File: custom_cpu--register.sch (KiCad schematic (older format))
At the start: 45 parts, among them P1 CONN_01X01, P10 CONN_01X01, P11 CONN_01X01, P12 CONN_01X01, P13 CONN_01X01, P14 CONN_01X01, P15 CONN_01X01, P16 CONN_01X01, P17 CONN_01X01, P18 CONN_01X01, P19 CONN_01X01, P2 CONN_01X01, P20 CONN_01X01, P21 CONN_01X01, P22 CONN_01X01, P23 CONN_01X01, P24 CONN_01X01, P25 CONN_01X01, P3 CONN_01X01, P4 CONN_01X01, P5 CONN_01X01, P6 CONN_01X01, P7 CONN_01X01, P8 CONN_01X01, P9 CONN_01X01, U1 74LS173, U2 74LS173, U3 74LS245

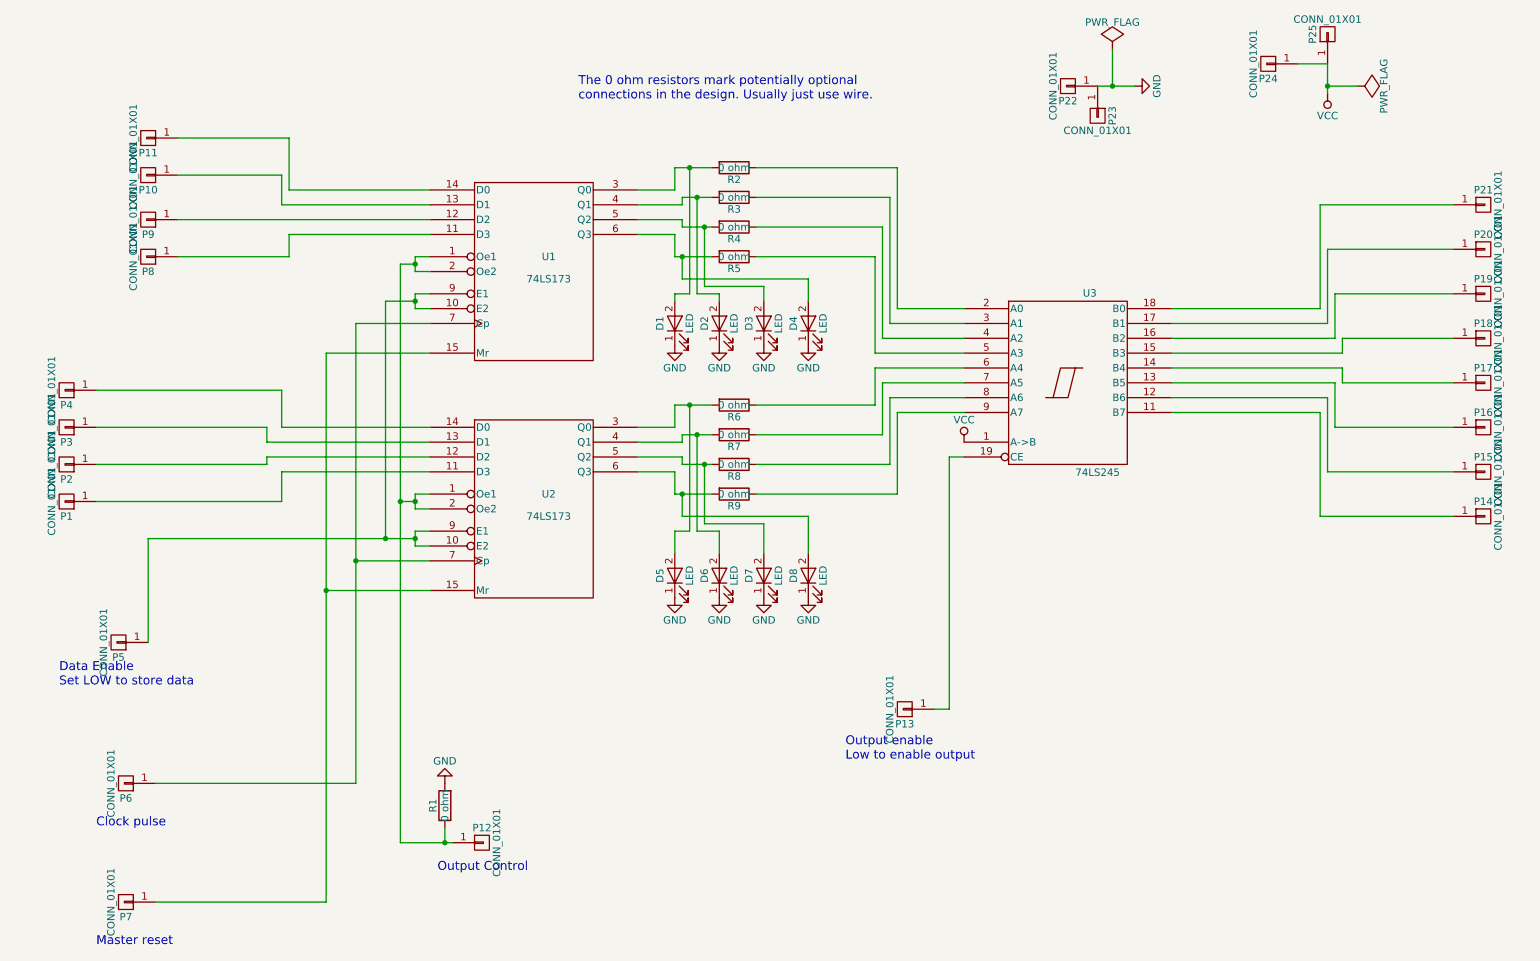
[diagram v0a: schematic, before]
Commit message: Make labels consistent with original design, add README
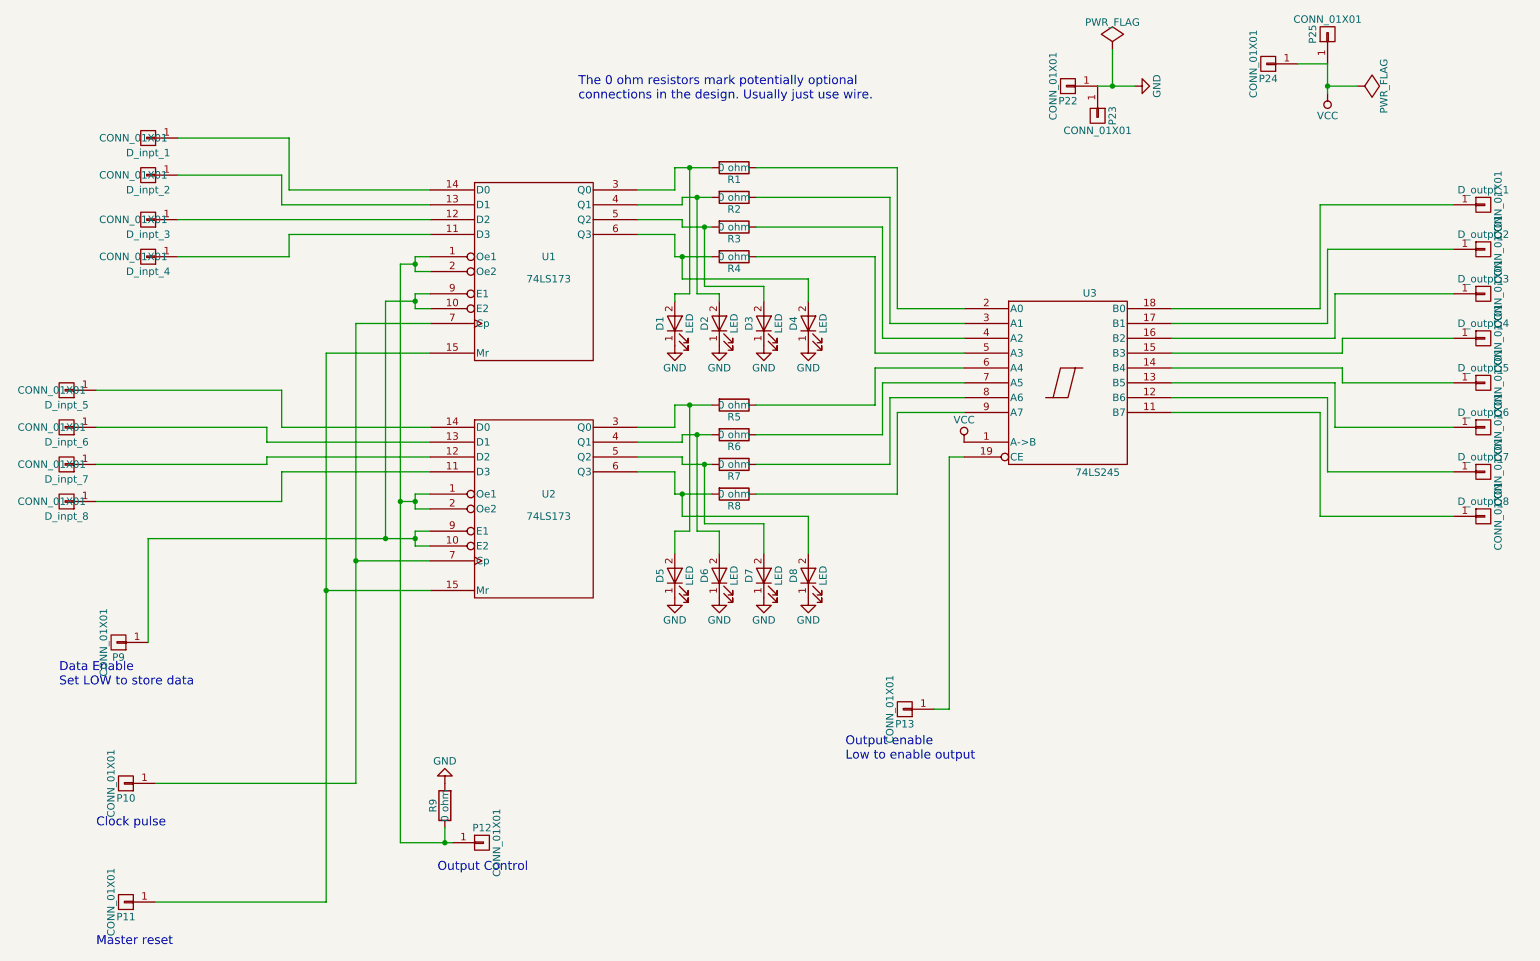
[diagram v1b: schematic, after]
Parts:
- renumbered P11 to D_inpt_1, P10 to D_inpt_2, P9 to D_inpt_3, P8 to D_inpt_4, P4 to D_inpt_5, P3 to D_inpt_6, P2 to D_inpt_7, P1 to D_inpt_8, P21 to D_outpt_1, P20 to D_outpt_2, P19 to D_outpt_3, P18 to D_outpt_4, P17 to D_outpt_5, P16 to D_outpt_6, P15 to D_outpt_7, P14 to D_outpt_8, P6 to P10, P7 to P11, P5 to P9, R2 to R1, R3 to R2, R4 to R3, R5 to R4, R6 to R5, R7 to R6, R8 to R7, R9 to R8, R1 to R9

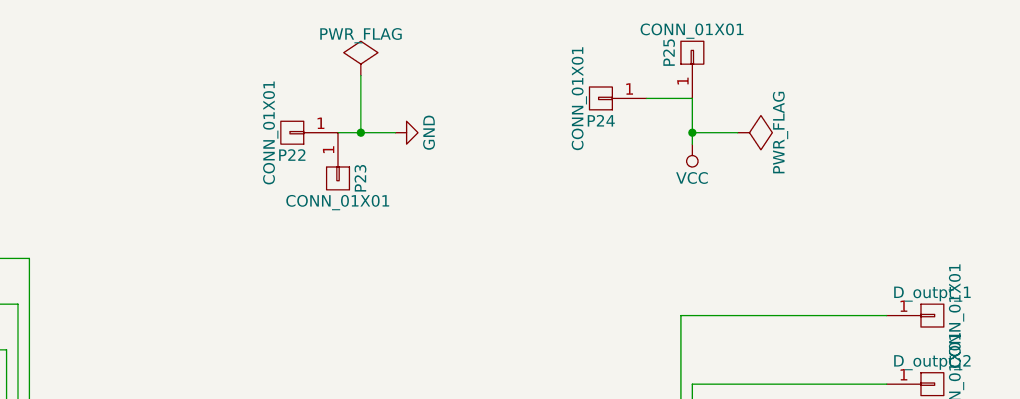
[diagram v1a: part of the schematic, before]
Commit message: Added redundant power pads to back of board
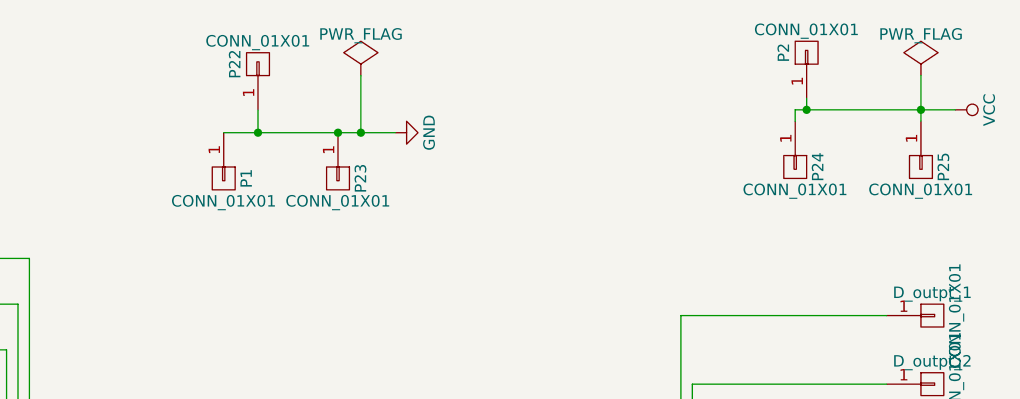
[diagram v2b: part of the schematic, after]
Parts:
- added P1, P2: CONN_01X01, Wire_Pads:SolderWirePad_single_SMD_5x10mm, symbol CONN_01X01
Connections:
- net GND: now also P1.1 (P1)
- net VCC: now also P2.1 (P1)
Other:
- moved on the sheet: P22, P24, P25
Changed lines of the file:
@@
 $EndComp
 $Comp
-L GND #PWR1
+L GND #PWR01
 U 1 1 58E818E9
 P 3300 5750
-F 0 "#PWR1" H 3300 5500 50  0001 C CNN
+F 0 "#PWR01" H 3300 5500 50  0001 C CNN
 F 1 "GND" H 3300 5600 50  0000 C CNN
 F 2 "" H 3300 5750 50  0000 C CNN
@@
 $EndComp
 $Comp
-L VCC #PWR10
+L VCC #PWR02
 U 1 1 58E831EF
 P 6800 3450
-F 0 "#PWR10" H 6800 3300 50  0001 C CNN
+F 0 "#PWR02" H 6800 3300 50  0001 C CNN
 F 1 "VCC" H 6800 3600 50  0000 C CNN
 F 2 "" H 6800 3450 50  0000 C CNN
@@
 $EndComp
 $Comp
-L GND #PWR11
+L GND #PWR03
 U 1 1 58E81990
 P 7950 1050
-F 0 "#PWR11" H 7950 800 50  0001 C CNN
+F 0 "#PWR03" H 7950 800 50  0001 C CNN
 F 1 "GND" H 7950 900 50  0000 C CNN
 F 2 "" H 7950 1050 50  0000 C CNN
@@
 L CONN_01X01 P22
 U 1 1 58E81B2E
-P 7500 1050
-F 0 "P22" H 7500 1150 50  0000 C CNN
-F 1 "CONN_01X01" V 7600 1050 50  0000 C CNN
-F 2 "Connectors:PINTST" H 7500 1050 50  0001 C CNN
-F 3 "" H 7500 1050 50  0000 C CNN
-	1    7500 1050
-	-1   0    0    1
+P 7350 750
+F 0 "P22" H 7350 850 50  0000 C CNN
+F 1 "CONN_01X01" V 7450 750 50  0000 C CNN
+F 2 "Connectors:PINTST" H 7350 750 50  0001 C CNN
+F 3 "" H 7350 750 50  0000 C CNN
+	1    7350 750
+	0    -1   -1   0
 $EndComp
 $Comp
@@
 $EndComp
 $Comp
-L PWR_FLAG #FLG2
+L PWR_FLAG #FLG04
 U 1 1 58E81EC9
-P 9450 1050
-F 0 "#FLG2" H 9450 1145 50  0001 C CNN
-F 1 "PWR_FLAG" H 9450 1230 50  0000 C CNN
-F 2 "" H 9450 1050 50  0000 C CNN
-F 3 "" H 9450 1050 50  0000 C CNN
-	1    9450 1050
-	0    1    1    0
+P 10250 800
+F 0 "#FLG04" H 10250 895 50  0001 C CNN
+F 1 "PWR_FLAG" H 10250 980 50  0000 C CNN
+F 2 "" H 10250 800 50  0000 C CNN
+F 3 "" H 10250 800 50  0000 C CNN
+	1    10250 800
+	1    0    0    -1
 $EndComp
 $Comp
 L CONN_01X01 P25
 U 1 1 58E81F44
-P 9250 700
-F 0 "P25" H 9250 800 50  0000 C CNN
-F 1 "CONN_01X01" V 9350 700 50  0000 C CNN
-F 2 "Wire_Pads:SolderWirePad_single_SMD_5x10mm" H 9250 700 50  0001 C CNN
-F 3 "" H 9250 700 50  0000 C CNN
-	1    9250 700
-	0    -1   -1   0
+P 10250 1200
+F 0 "P25" H 10250 1300 50  0000 C CNN
+F 1 "CONN_01X01" V 10350 1200 50  0000 C CNN
+F 2 "Wire_Pads:SolderWirePad_single_SMD_5x10mm" H 10250 1200 50  0001 C CNN
+F 3 "" H 10250 1200 50  0000 C CNN
+	1    10250 1200
+	0    1    1    0
 $EndComp
 $Comp
 L CONN_01X01 P24
 U 1 1 58E82042
-P 8850 900
-F 0 "P24" H 8850 1000 50  0000 C CNN
-F 1 "CONN_01X01" V 8950 900 50  0000 C CNN
-F 2 "Connectors:PINTST" H 8850 900 50  0001 C CNN
-F 3 "" H 8850 900 50  0000 C CNN
-	1    8850 900
-	-1   0    0    1
-$EndComp
-$Comp
-L VCC #PWR12
+P 9700 1200
+F 0 "P24" H 9700 1300 50  0000 C CNN
+F 1 "CONN_01X01" V 9800 1200 50  0000 C CNN
+F 2 "Connectors:PINTST" H 9700 1200 50  0001 C CNN
+F 3 "" H 9700 1200 50  0000 C CNN
+	1    9700 1200
+	0    1    1    0
+$EndComp
+$Comp
+L VCC #PWR05
 U 1 1 58E820DA
-P 9250 1100
-F 0 "#PWR12" H 9250 950 50  0001 C CNN
-F 1 "VCC" H 9250 1250 50  0000 C CNN
-F 2 "" H 9250 1100 50  0000 C CNN
-F 3 "" H 9250 1100 50  0000 C CNN
-	1    9250 1100
-	-1   0    0    1
-$EndComp
-$Comp
-L PWR_FLAG #FLG1
+P 10400 950
+F 0 "#PWR05" H 10400 800 50  0001 C CNN
+F 1 "VCC" H 10400 1100 50  0000 C CNN
+F 2 "" H 10400 950 50  0000 C CNN
+F 3 "" H 10400 950 50  0000 C CNN
+	1    10400 950
+	0    1    1    0
+$EndComp
+$Comp
+L PWR_FLAG #FLG06
 U 1 1 58E8410D
 P 7800 800
-F 0 "#FLG1" H 7800 895 50  0001 C CNN
+F 0 "#FLG06" H 7800 895 50  0001 C CNN
 F 1 "PWR_FLAG" H 7800 980 50  0000 C CNN
 F 2 "" H 7800 800 50  0000 C CNN
@@
 $EndComp
 $Comp
-L GND #PWR2
+L GND #PWR07
 U 1 1 58E89432
 P 4850 2800
-F 0 "#PWR2" H 4850 2550 50  0001 C CNN
+F 0 "#PWR07" H 4850 2550 50  0001 C CNN
 F 1 "GND" H 4850 2650 50  0000 C CNN
 F 2 "" H 4850 2800 50  0000 C CNN
@@
 $EndComp
 $Comp
-L GND #PWR4
+L GND #PWR08
 U 1 1 58E894C4
 P 5150 2800
-F 0 "#PWR4" H 5150 2550 50  0001 C CNN
+F 0 "#PWR08" H 5150 2550 50  0001 C CNN
 F 1 "GND" H 5150 2650 50  0000 C CNN
 F 2 "" H 5150 2800 50  0000 C CNN
@@
 $EndComp
 $Comp
-L GND #PWR6
+L GND #PWR09
 U 1 1 58E89556
 P 5450 2800
-F 0 "#PWR6" H 5450 2550 50  0001 C CNN
+F 0 "#PWR09" H 5450 2550 50  0001 C CNN
 F 1 "GND" H 5450 2650 50  0000 C CNN
 F 2 "" H 5450 2800 50  0000 C CNN
@@
 $EndComp
 $Comp
-L GND #PWR8
+L GND #PWR010
 U 1 1 58E895E8
 P 5750 2800
-F 0 "#PWR8" H 5750 2550 50  0001 C CNN
+F 0 "#PWR010" H 5750 2550 50  0001 C CNN
 F 1 "GND" H 5750 2650 50  0000 C CNN
 F 2 "" H 5750 2800 50  0000 C CNN
@@
 $EndComp
 $Comp
-L GND #PWR9
+L GND #PWR011
 U 1 1 58E8967A
 P 5750 4500
-F 0 "#PWR9" H 5750 4250 50  0001 C CNN
+F 0 "#PWR011" H 5750 4250 50  0001 C CNN
 F 1 "GND" H 5750 4350 50  0000 C CNN
 F 2 "" H 5750 4500 50  0000 C CNN
@@
 $EndComp
 $Comp
-L GND #PWR7
+L GND #PWR012
 U 1 1 58E8970C
 P 5450 4500
-F 0 "#PWR7" H 5450 4250 50  0001 C CNN
+F 0 "#PWR012" H 5450 4250 50  0001 C CNN
 F 1 "GND" H 5450 4350 50  0000 C CNN
 F 2 "" H 5450 4500 50  0000 C CNN
@@
 $EndComp
 $Comp
-L GND #PWR5
+L GND #PWR013
 U 1 1 58E8979E
 P 5150 4500
-F 0 "#PWR5" H 5150 4250 50  0001 C CNN
+F 0 "#PWR013" H 5150 4250 50  0001 C CNN
 F 1 "GND" H 5150 4350 50  0000 C CNN
 F 2 "" H 5150 4500 50  0000 C CNN
@@
 $EndComp
 $Comp
-L GND #PWR3
+L GND #PWR014
 U 1 1 58E89830
 P 4850 4500
-F 0 "#PWR3" H 4850 4250 50  0001 C CNN
+F 0 "#PWR014" H 4850 4250 50  0001 C CNN
 F 1 "GND" H 4850 4350 50  0000 C CNN
 F 2 "" H 4850 4500 50  0000 C CNN
@@
 	9200 3950 10100 3950
 Wire Wire Line
-	7700 1050 7950 1050
-Wire Wire Line
-	9450 1050 9250 1050
-Wire Wire Line
-	9250 900  9250 1100
-Connection ~ 9250 1050
-Wire Wire Line
-	9250 900  9050 900
+	7200 1050 7950 1050
 Wire Wire Line
 	3300 6150 3300 6050
@@
 	5750 2350 5750 2500
 Connection ~ 4900 2200
+$Comp
+L CONN_01X01 P2
+U 1 1 58EB199F
+P 9750 700
+F 0 "P2" H 9750 800 50  0000 C CNN
+F 1 "CONN_01X01" V 9850 700 50  0000 C CNN
+F 2 "Wire_Pads:SolderWirePad_single_SMD_5x10mm" H 9750 700 50  0001 C CNN
+F 3 "" H 9750 700 50  0000 C CNN
+	1    9750 700
+	0    -1   -1   0
+$EndComp
+$Comp
+L CONN_01X01 P1
+U 1 1 58EB1AE9
+P 7200 1250
+F 0 "P1" H 7200 1350 50  0000 C CNN
+F 1 "CONN_01X01" V 7300 1250 50  0000 C CNN
+F 2 "Wire_Pads:SolderWirePad_single_SMD_5x10mm" H 7200 1250 50  0001 C CNN
+F 3 "" H 7200 1250 50  0000 C CNN
+	1    7200 1250
+	0    1    1    0
+$EndComp
+Connection ~ 7700 1050
+Wire Wire Line
+	7350 950  7350 1050
+Connection ~ 7350 1050
+Wire Wire Line
+	9750 900  9750 950
+Wire Wire Line
+	9700 950  10400 950
+Wire Wire Line
+	10250 800  10250 1000
+Connection ~ 10250 950
+Wire Wire Line
+	9700 1000 9700 950
+Connection ~ 9750 950
 $EndSCHEMATC
